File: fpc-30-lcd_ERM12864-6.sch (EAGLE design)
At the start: 21 parts

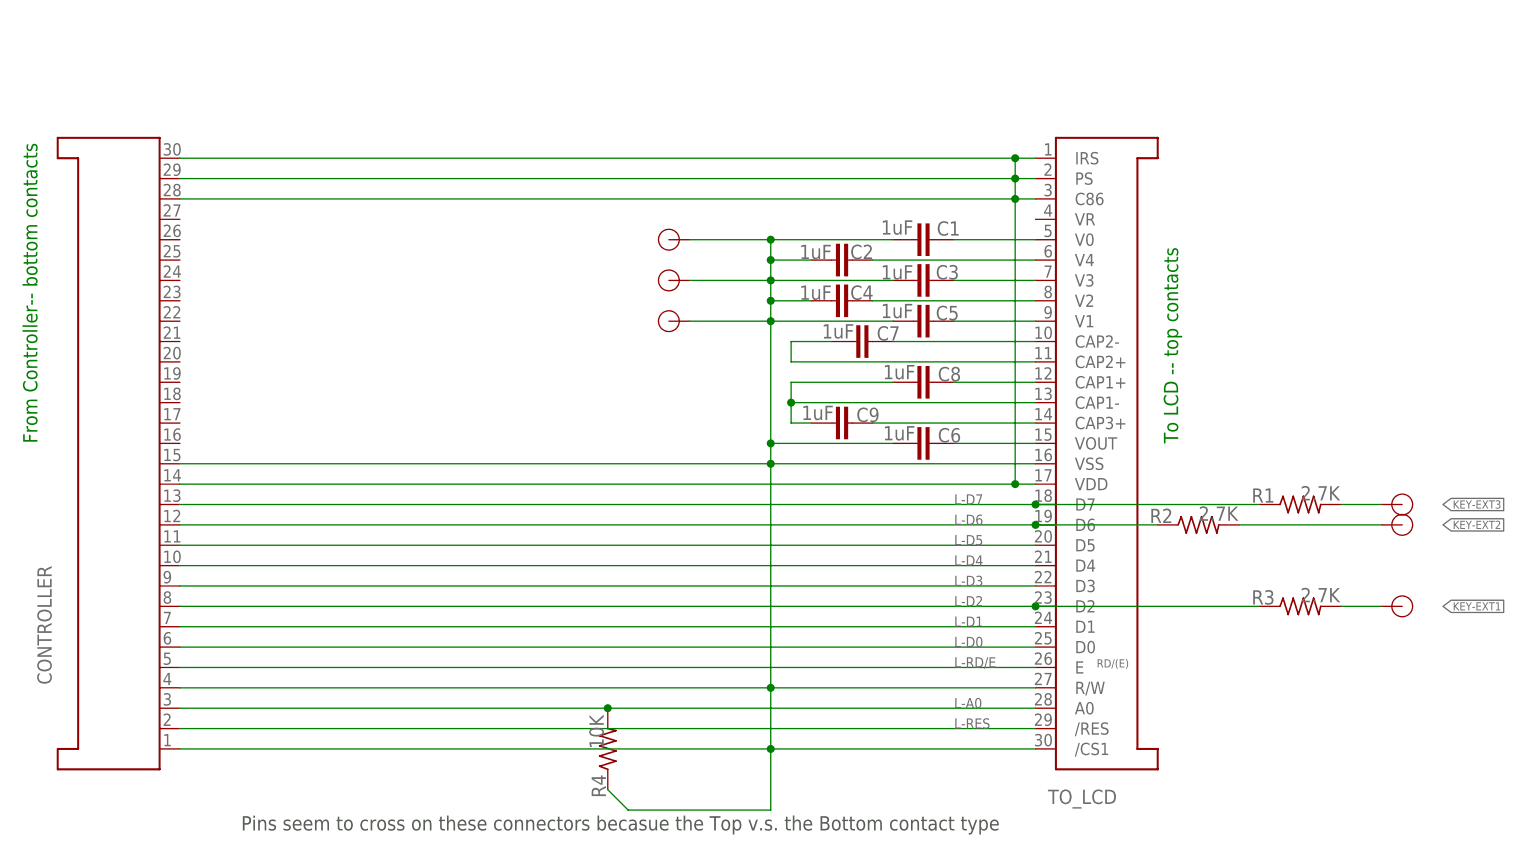
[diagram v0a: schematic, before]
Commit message: added pictures and docs added firmware binary added old JR9303 wiring and pin-out doc added lcd display adapter patch boards for different displays
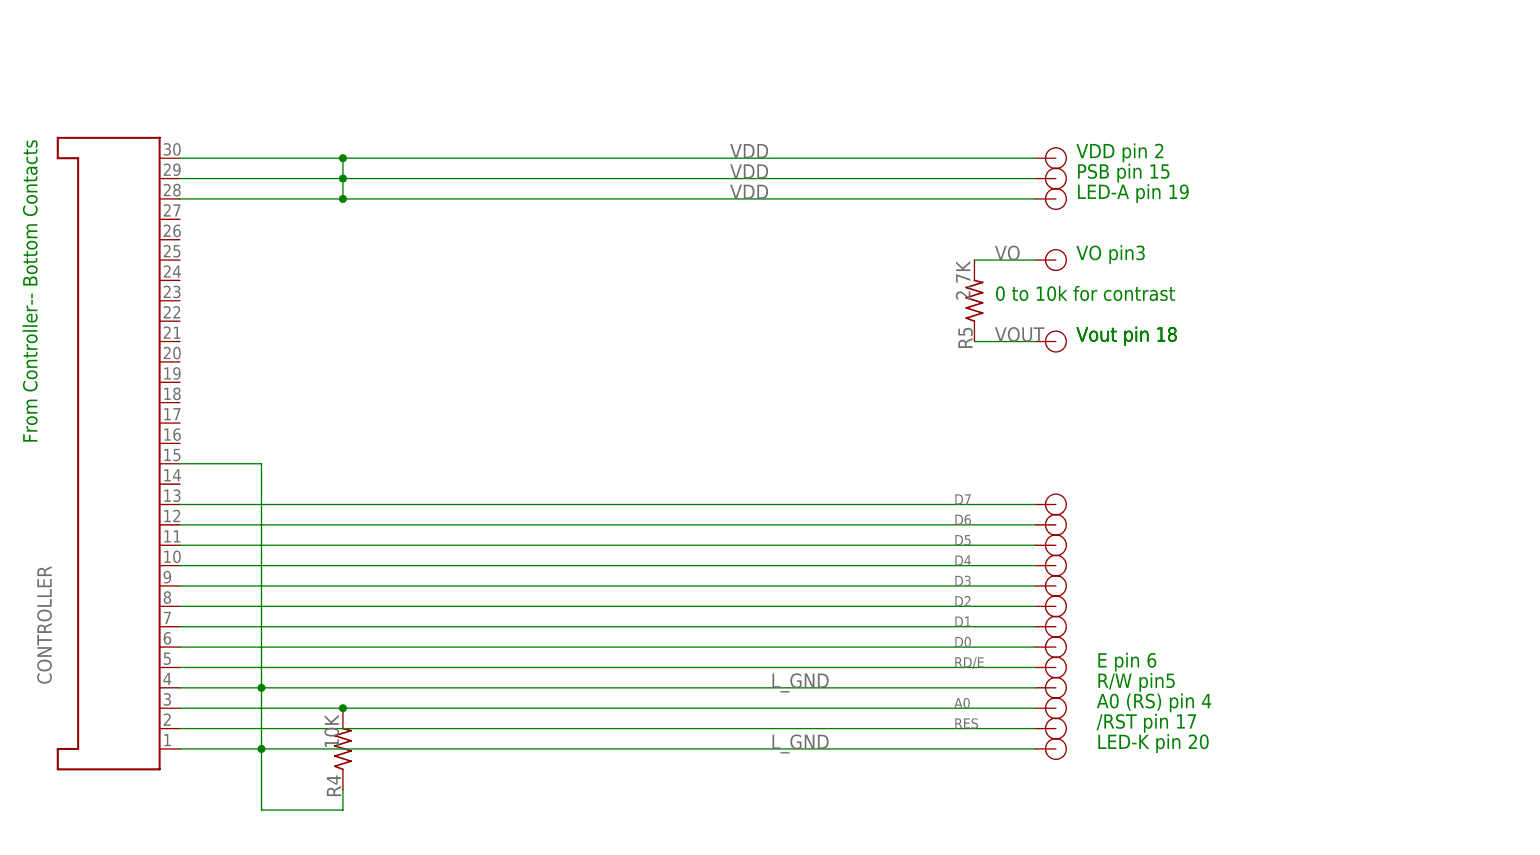
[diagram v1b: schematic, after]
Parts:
- removed C1, C2, C3, C4, C5, C6, C7, C8, C9: 1uF, rcl:C-EUC0805
- removed EXT1, EXT2, EXT3, K_EXT4, K_EXT5, K_EXT6: TP-1, XP9300:TP-1
- removed R1, R2, R3: 2.7K, rcl:R-US_R0603
- removed TO_LCD: FPC30 - Bottom-pins, XP9300:FPC_30_ERC12864-2
- added /RST, A0/RS, D1, D2, D3, D4, D5, D6, LED_A, LED_K, PSB, R/W, RD/E, VDD: TP-1, XP9300:TP-1
- added D0, D7, VO, VOUT: D7, XP9300:TP-1
- added R5: 2.7K, rcl:R-US_R0603
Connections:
- removed net KEY-EXT1: EXT1.P$1, R3.2
- removed net KEY-EXT2: EXT2.P$1, R2.2
- removed net KEY-EXT3: EXT3.P$1, R1.2
- removed net L-A0: CONTROLLER.P$3, R4.2, TO_LCD.A0
- removed net L-D0: CONTROLLER.P$6, TO_LCD.D0
- removed net L-D1: CONTROLLER.P$7, TO_LCD.D1
- removed net L-D2: CONTROLLER.P$8, R3.1, TO_LCD.D2
- removed net L-D3: CONTROLLER.P$9, TO_LCD.D3
- removed net L-D4: CONTROLLER.P$10, TO_LCD.D4
- removed net L-D5: CONTROLLER.P$11, TO_LCD.D5
- removed net L-D6: CONTROLLER.P$12, R2.1, TO_LCD.D6
- removed net L-D7: CONTROLLER.P$13, R1.1, TO_LCD.D7
- removed net L-RD/E: CONTROLLER.P$5, TO_LCD.E
- removed net L-RES: CONTROLLER.P$2, TO_LCD./RES
- removed net L_VDD: CONTROLLER.P$14, CONTROLLER.P$28, CONTROLLER.P$29, CONTROLLER.P$30, TO_LCD.C86, TO_LCD.IRS, TO_LCD.PS, TO_LCD.VDD
- removed net N$10: C7.2, TO_LCD.CAP2+
- removed net N$11: C8.2, C9.2, TO_LCD.CAP1-
- removed net N$12: C8.1, TO_LCD.CAP1+
- removed net N$14: C9.1, TO_LCD.CAP3+
- removed net N$15: C6.1, TO_LCD.VOUT
- removed net N$3: C1.1, TO_LCD.V0
- removed net N$4: C2.1, TO_LCD.V4
- removed net N$5: C3.1, TO_LCD.V3
- removed net N$6: C4.1, TO_LCD.V2
- removed net N$7: C5.1, TO_LCD.V1
- removed net N$9: C7.1, TO_LCD.CAP2-
- new net A0: A0/RS.P$1, CONTROLLER.P$3, R4.2
- new net D0: CONTROLLER.P$6, D0.P$1
- new net D1: CONTROLLER.P$7, D1.P$1
- new net D2: CONTROLLER.P$8, D2.P$1
- new net D3: CONTROLLER.P$9, D3.P$1
- new net D4: CONTROLLER.P$10, D4.P$1
- new net D5: CONTROLLER.P$11, D5.P$1
- new net D6: CONTROLLER.P$12, D6.P$1
- new net D7: CONTROLLER.P$13, D7.P$1
- new net RD/E: CONTROLLER.P$5, RD/E.P$1
- new net RES: /RST.P$1, CONTROLLER.P$2
- new net VDD: CONTROLLER.P$28, CONTROLLER.P$29, CONTROLLER.P$30, LED_A.P$1, PSB.P$1, VDD.P$1
- new net VO: R5.2, VO.P$1
- new net VOUT: R5.1, VOUT.P$1
- net L_GND: now also LED_K.P$1, R/W.P$1; no longer C1.2, C2.2, C3.2, C4.2, C5.2, C6.2, K_EXT4.P$1, K_EXT5.P$1, K_EXT6.P$1, TO_LCD./CS1, TO_LCD.R/W, TO_LCD.VSS
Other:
- note added: "/RST pin 17"
- note added: "0 to 10k for contrast"
- note added: "A0 (RS) pin 4"
- note added: "E pin 6"
- note added: "From Controller-- Bottom Contacts"
- note added: "LED-A pin 19"
- note added: "LED-K pin 20"
- note added: "PSB pin 15"
- note added: "R/W pin5"
- note added: "VDD pin 2"
- note added: "VO pin3"
- note added: "Vout pin 18"
- note removed: "From Controller-- bottom contacts"
- note removed: "Pins seem to cross on these connectors becasue the Top v.s. the Bottom contact type"
- note removed: "RD/(E)"
- note removed: "To LCD -- top contacts"
- moved on the sheet: R4
